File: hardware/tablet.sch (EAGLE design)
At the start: 16 parts, among them IC2 MCP3201, IC3 DG9233EDY, IC4 MAX6104EUR

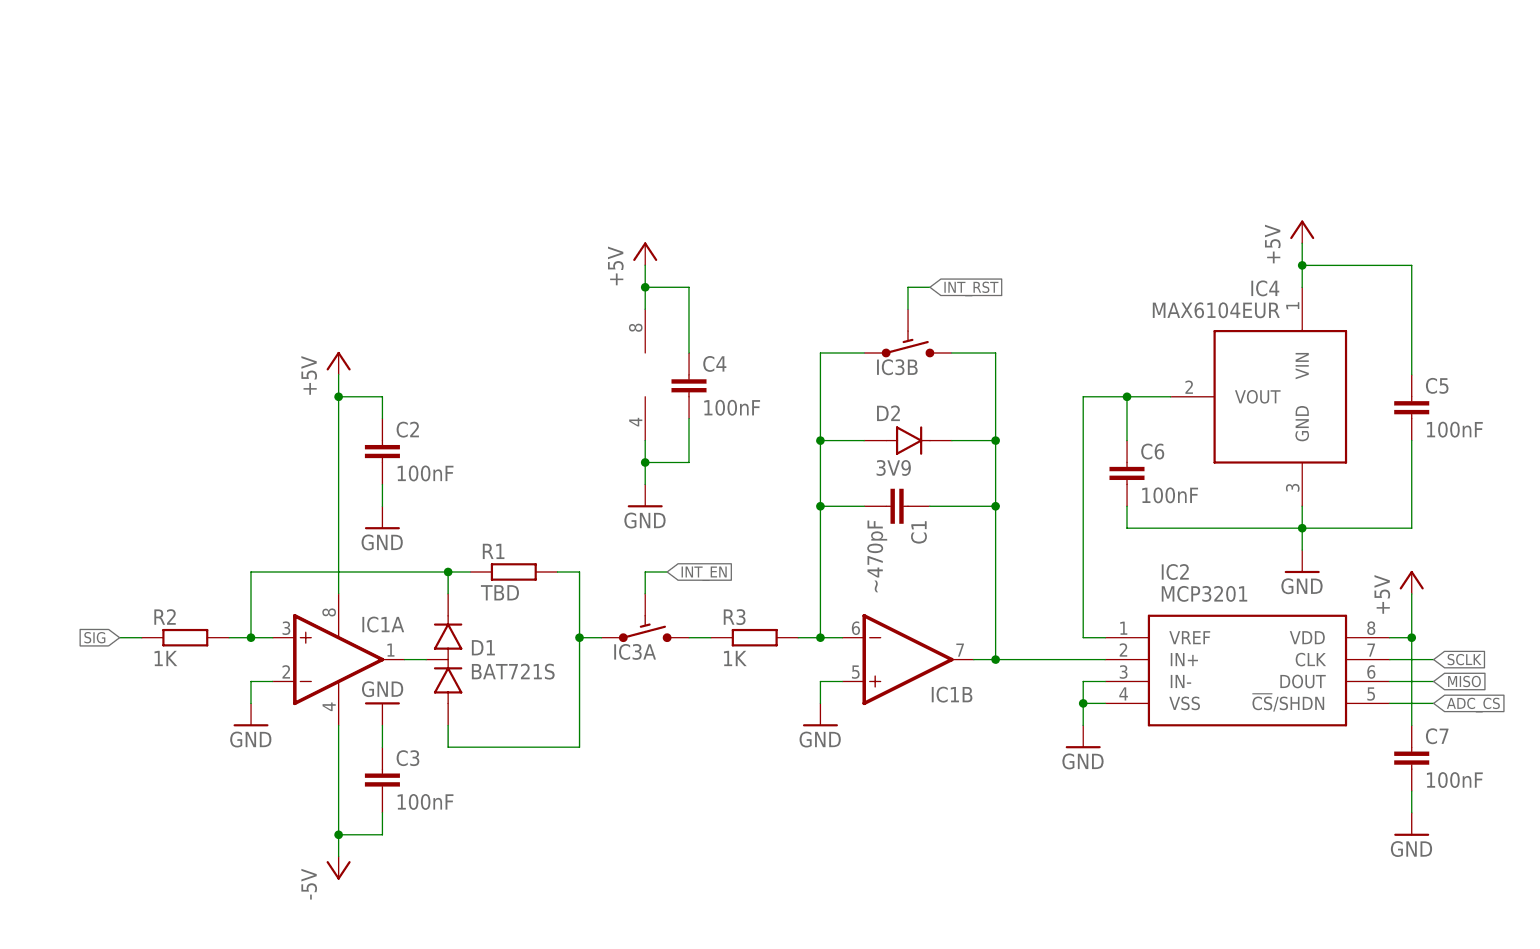
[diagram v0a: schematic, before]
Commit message: Simplify analog switch layout and increase analog ref load capacitance to ensure stability
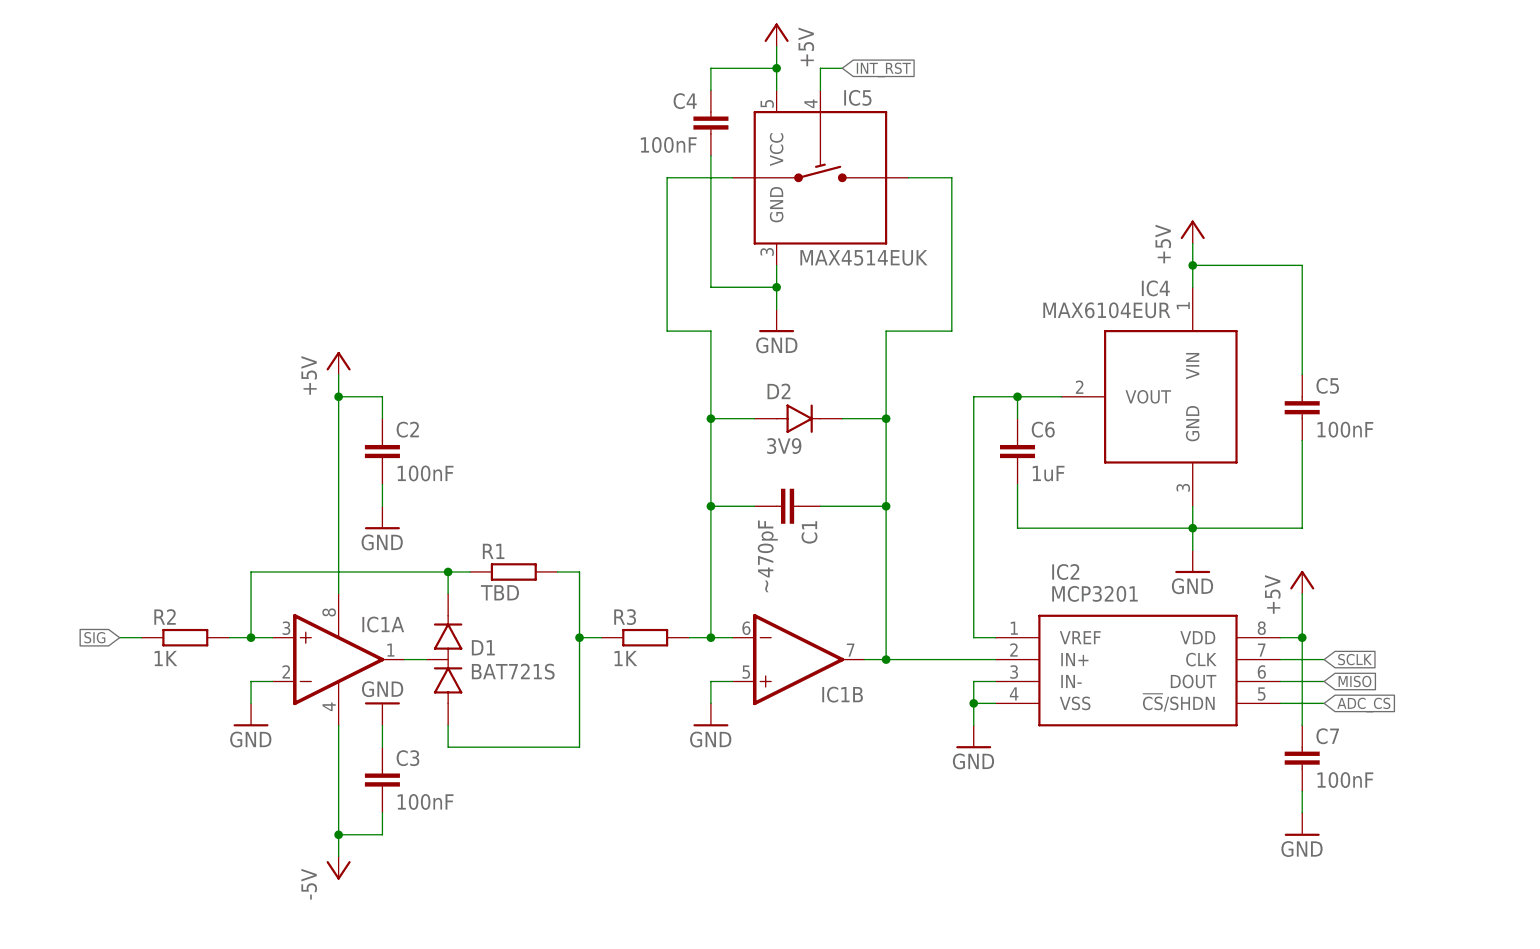
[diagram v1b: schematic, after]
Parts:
- removed IC3: DG9233EDY, 0jpe:DG9233EDY
- added IC5: MAX4514EUK, 0jpe:MAX4514EUK
- C6: value 100nF -> 1uF
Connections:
- removed net INT_EN: IC3A.SEL
- removed net N$7: IC3A.NO, R3.1
- net +5V: now also IC5.VCC; no longer IC3PWR.V+
- net GND: now also IC5.GND; no longer IC3PWR.V-
- net INT_RST: now also IC5.IN; no longer IC3B.SEL
- net N$1: now also R3.1; no longer IC3A.COM
- net N$4: now also IC5.COM; no longer IC3B.COM
- net VOUT: now also IC5.NO; no longer IC3B.NO
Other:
- moved on the sheet: C1, C4, C5, C6, C7, D2, IC1B, IC2, IC4, R3

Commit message: Add protection diodes to common signal
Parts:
- added D3, D4: 5V1, 0jpe:DSOD323
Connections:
- new net N$5: D3.2, D4.2
- net GND: now also D3.1
- net SIG: now also D4.1
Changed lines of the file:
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@@
 <grid distance="0.1" unitdist="inch" unit="inch" style="lines" multiple="1" display="no" altdistance="0.01" altunitdist="inch" altunit="inch"/>
 <layers>
-<layer number="1" name="Top" color="4" fill="1" visible="no" active="no"/>
-<layer number="2" name="Route2" color="1" fill="3" visible="no" active="no"/>
-<layer number="3" name="Route3" color="4" fill="3" visible="no" active="no"/>
-<layer number="4" name="Route4" color="1" fill="4" visible="no" active="no"/>
-<layer number="5" name="Route5" color="4" fill="4" visible="no" active="no"/>
-<layer number="6" name="Route6" color="1" fill="8" visible="no" active="no"/>
-<layer number="7" name="Route7" color="4" fill="8" visible="no" active="no"/>
-<layer number="8" name="Route8" color="1" fill="2" visible="no" active="no"/>
-<layer number="9" name="Route9" color="4" fill="2" visible="no" active="no"/>
-<layer number="10" name="Route10" color="1" fill="7" visible="no" active="no"/>
-<layer number="11" name="Route11" color="4" fill="7" visible="no" active="no"/>
-<layer number="12" name="Route12" color="1" fill="5" visible="no" active="no"/>
-<layer number="13" name="Route13" color="4" fill="5" visible="no" active="no"/>
-<layer number="14" name="Route14" color="1" fill="6" visible="no" active="no"/>
-<layer number="15" name="Route15" color="4" fill="6" visible="no" active="no"/>
-<layer number="16" name="Bottom" color="1" fill="1" visible="no" active="no"/>
-<layer number="17" name="Pads" color="2" fill="1" visible="no" active="no"/>
-<layer number="18" name="Vias" color="2" fill="1" visible="no" active="no"/>
-<layer number="19" name="Unrouted" color="6" fill="1" visible="no" active="no"/>
-<layer number="20" name="Dimension" color="24" fill="1" visible="no" active="no"/>
-<layer number="21" name="tPlace" color="7" fill="1" visible="no" active="no"/>
-<layer number="22" name="bPlace" color="7" fill="1" visible="no" active="no"/>
-<layer number="23" name="tOrigins" color="15" fill="1" visible="no" active="no"/>
-<layer number="24" name="bOrigins" color="15" fill="1" visible="no" active="no"/>
-<layer number="25" name="tNames" color="7" fill="1" visible="no" active="no"/>
-<layer number="26" name="bNames" color="7" fill="1" visible="no" active="no"/>
-<layer number="27" name="tValues" color="7" fill="1" visible="no" active="no"/>
-<layer number="28" name="bValues" color="7" fill="1" visible="no" active="no"/>
+<layer number="1" name="Top" color="4" fill="1" visible="yes" active="no"/>
+<layer number="2" name="Route2" color="1" fill="3" visible="yes" active="no"/>
+<layer number="3" name="Route3" color="4" fill="3" visible="yes" active="no"/>
+<layer number="4" name="Route4" color="1" fill="4" visible="yes" active="no"/>
+<layer number="5" name="Route5" color="4" fill="4" visible="yes" active="no"/>
+<layer number="6" name="Route6" color="1" fill="8" visible="yes" active="no"/>
+<layer number="7" name="Route7" color="4" fill="8" visible="yes" active="no"/>
+<layer number="8" name="Route8" color="1" fill="2" visible="yes" active="no"/>
+<layer number="9" name="Route9" color="4" fill="2" visible="yes" active="no"/>
+<layer number="10" name="Route10" color="1" fill="7" visible="yes" active="no"/>
+<layer number="11" name="Route11" color="4" fill="7" visible="yes" active="no"/>
+<layer number="12" name="Route12" color="1" fill="5" visible="yes" active="no"/>
+<layer number="13" name="Route13" color="4" fill="5" visible="yes" active="no"/>
+<layer number="14" name="Route14" color="1" fill="6" visible="yes" active="no"/>
+<layer number="15" name="Route15" color="4" fill="6" visible="yes" active="no"/>
+<layer number="16" name="Bottom" color="1" fill="1" visible="yes" active="no"/>
+<layer number="17" name="Pads" color="2" fill="1" visible="yes" active="no"/>
+<layer number="18" name="Vias" color="2" fill="1" visible="yes" active="no"/>
+<layer number="19" name="Unrouted" color="6" fill="1" visible="yes" active="no"/>
+<layer number="20" name="Dimension" color="24" fill="1" visible="yes" active="no"/>
+<layer number="21" name="tPlace" color="7" fill="1" visible="yes" active="no"/>
+<layer number="22" name="bPlace" color="7" fill="1" visible="yes" active="no"/>
+<layer number="23" name="tOrigins" color="15" fill="1" visible="yes" active="no"/>
+<layer number="24" name="bOrigins" color="15" fill="1" visible="yes" active="no"/>
+<layer number="25" name="tNames" color="7" fill="1" visible="yes" active="no"/>
+<layer number="26" name="bNames" color="7" fill="1" visible="yes" active="no"/>
+<layer number="27" name="tValues" color="7" fill="1" visible="yes" active="no"/>
+<layer number="28" name="bValues" color="7" fill="1" visible="yes" active="no"/>
 <layer number="29" name="tStop" color="7" fill="3" visible="no" active="no"/>
 <layer number="30" name="bStop" color="7" fill="6" visible="no" active="no"/>
@@
 <layer number="35" name="tGlue" color="7" fill="4" visible="no" active="no"/>
 <layer number="36" name="bGlue" color="7" fill="5" visible="no" active="no"/>
-<layer number="37" name="tTest" color="7" fill="1" visible="no" active="no"/>
-<layer number="38" name="bTest" color="7" fill="1" visible="no" active="no"/>
+<layer number="37" name="tTest" color="7" fill="1" visible="yes" active="no"/>
+<layer number="38" name="bTest" color="7" fill="1" visible="yes" active="no"/>
 <layer number="39" name="tKeepout" color="4" fill="11" visible="no" active="no"/>
 <layer number="40" name="bKeepout" color="1" fill="11" visible="no" active="no"/>
@@
 <layer number="44" name="Drills" color="7" fill="1" visible="no" active="no"/>
 <layer number="45" name="Holes" color="7" fill="1" visible="no" active="no"/>
-<layer number="46" name="Milling" color="3" fill="1" visible="no" active="no"/>
-<layer number="47" name="Measures" color="7" fill="1" visible="no" active="no"/>
-<layer number="48" name="Document" color="7" fill="1" visible="no" active="no"/>
-<layer number="49" name="Reference" color="7" fill="1" visible="no" active="no"/>
-<layer number="51" name="tDocu" color="7" fill="1" visible="no" active="no"/>
-<layer number="52" name="bDocu" color="7" fill="1" visible="no" active="no"/>
+<layer number="46" name="Milling" color="3" fill="1" visible="yes" active="no"/>
+<layer number="47" name="Measures" color="7" fill="1" visible="yes" active="no"/>
+<layer number="48" name="Document" color="7" fill="1" visible="yes" active="no"/>
+<layer number="49" name="Reference" color="7" fill="1" visible="yes" active="no"/>
+<layer number="51" name="tDocu" color="7" fill="1" visible="yes" active="no"/>
+<layer number="52" name="bDocu" color="7" fill="1" visible="yes" active="no"/>
 <layer number="88" name="SimResults" color="9" fill="1" visible="yes" active="yes"/>
 <layer number="89" name="SimProbes" color="9" fill="1" visible="yes" active="yes"/>
@@
 <part name="GND8" library="supply1" library_urn="urn:adsk.eagle:library:371" deviceset="GND" device=""/>
 <part name="IC5" library="0jpe" deviceset="MAX4514" device="EUK"/>
+<part name="D3" library="0jpe" deviceset="D" device="SOD323" value="5V1"/>
+<part name="D4" library="0jpe" deviceset="D" device="SOD323" value="5V1"/>
+<part name="GND9" library="supply1" library_urn="urn:adsk.eagle:library:371" deviceset="GND" device=""/>
 </parts>
 <sheets>
@@
 <instance part="GND8" gate="1" x="111.76" y="-20.32"/>
 <instance part="IC5" gate="G$1" x="55.88" y="55.88"/>
+<instance part="D3" gate="G$1" x="-27.94" y="-17.78" rot="R90"/>
+<instance part="D4" gate="G$1" x="-27.94" y="-5.08" rot="R270"/>
+<instance part="GND9" gate="1" x="-27.94" y="-27.94"/>
 </instances>
 <busses>
@@
 <wire x1="111.76" y1="-17.78" x2="111.76" y2="-15.24" width="0.1524" layer="91"/>
 </segment>
+<segment>
+<pinref part="D3" gate="G$1" pin="1"/>
+<pinref part="GND9" gate="1" pin="GND"/>
+<wire x1="-27.94" y1="-22.86" x2="-27.94" y2="-25.4" width="0.1524" layer="91"/>
+</segment>
 </net>
 <net name="SIG" class="0">
 <segment>
 <pinref part="R2" gate="G$1" pin="1"/>
-<wire x1="-22.86" y1="2.54" x2="-25.4" y2="2.54" width="0.1524" layer="91"/>
-<label x="-25.4" y="2.54" size="1.27" layer="95" rot="R180" xref="yes"/>
+<wire x1="-22.86" y1="2.54" x2="-27.94" y2="2.54" width="0.1524" layer="91"/>
+<label x="-30.48" y="2.54" size="1.27" layer="95" rot="R180" xref="yes"/>
+<pinref part="D4" gate="G$1" pin="1"/>
+<wire x1="-27.94" y1="2.54" x2="-30.48" y2="2.54" width="0.1524" layer="91"/>
+<wire x1="-27.94" y1="2.54" x2="-27.94" y2="0" width="0.1524" layer="91"/>
+<junction x="-27.94" y="2.54"/>
 </segment>
 </net>
@@
 </segment>
 </net>
+<net name="N$5" class="0">
+<segment>
+<pinref part="D4" gate="G$1" pin="2"/>
+<pinref part="D3" gate="G$1" pin="2"/>
+<wire x1="-27.94" y1="-10.16" x2="-27.94" y2="-12.7" width="0.1524" layer="91"/>
+</segment>
+</net>

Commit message: Fix precision rectifier op amp orientation
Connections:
- net GND: now also IC1A.+IN; no longer IC1A.-IN
- net N$2: now also IC1A.-IN; no longer IC1A.+IN
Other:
- moved on the sheet: IC1A
